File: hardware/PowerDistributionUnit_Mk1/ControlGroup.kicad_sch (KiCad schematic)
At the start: 12 parts, among them U7 74LVC594APW,118

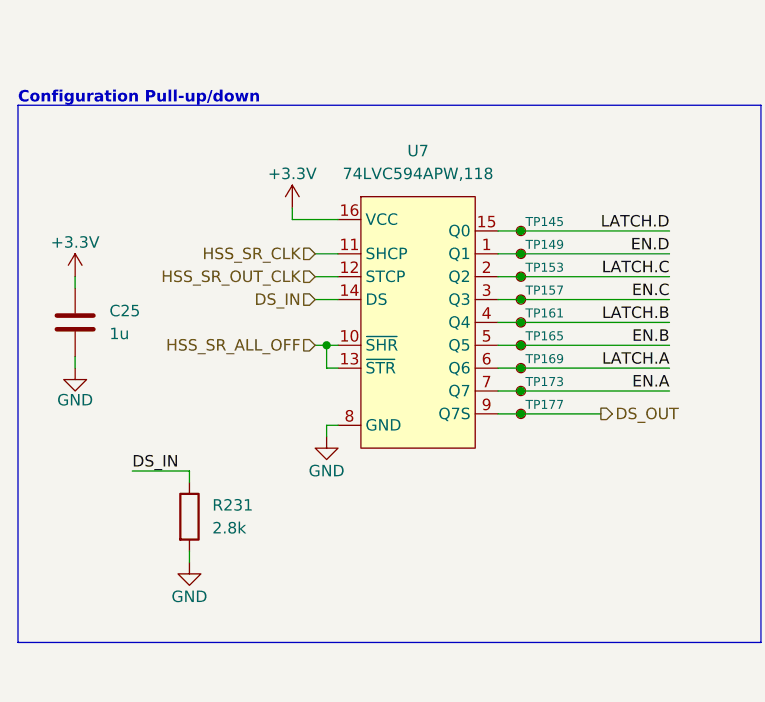
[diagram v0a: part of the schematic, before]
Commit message: BBPDU Mk1 RevB (#6)
* update adc reference to use internal reference (open) with jumper option

* change ADC - reading voltage to resistor divider with option to reference to GND or 1.65V

* change ADC AVDD and AGND connections to regular 3.3V and GND

* make input protection use b2b FETs

* update KiCad-Sharepoint

* update LeaderSOM symbol and SPI pinout (bottom) - need to swap SPI2 and SPI3 names, remove local library copy of LeaderSOM symbol

* change LSOM footprint to centered LSOM footprint, make centered LSOM footprint plated to address hidden pins on LSOM symbol

* update PCB from schematic

* layout/routing for input protection

* fix centered LSOM footprint 3D model, update footprint

* reroute LSOM SPI connections, repin logic analyzer connections

* reroute updated AVDD and AGND on ADCs

* reroute ADCIN- connections to resistor divider from 3.3VA (for 1.65V or 0V)

* change jumper to DNP resistor for ADC reference, routed

* route a couple of missed connections (LV in connection to input prot IC, LV sense connection)

* address DRC

* fix silkscreen labelling issues

* add SRCLK_ENed connection to logic analyzer connector

* silkscreen fixes and stuff

* update rev and year label

* address DRC

* update schematic documentation, clean up, update titleblocks

* add LCSC P/N to libs

* update all symbols with LCSC P/N

* update PCB with LCSC P/Ns

* add center mounting hole

* correct SR part number to SOIC package

* correct fuse table

* change lv sense rdiv values to avoid extended components, update all pull-ups/-downs using 2.8k

* rotate nanofits for inwards clip

* NC the mounting holes (because Lakshay Gupta)

* fix shorted nets error from wrong size res symbol from resistor change

* address DRC

* assembly setup, change latch pull resistor DNP to latch off instead of auto retry by default

* silkscreen stuff

* change DNP for HSS diagnostics to default to current

* change DNP to disable HSS diagnostics by default (primarily use external current 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
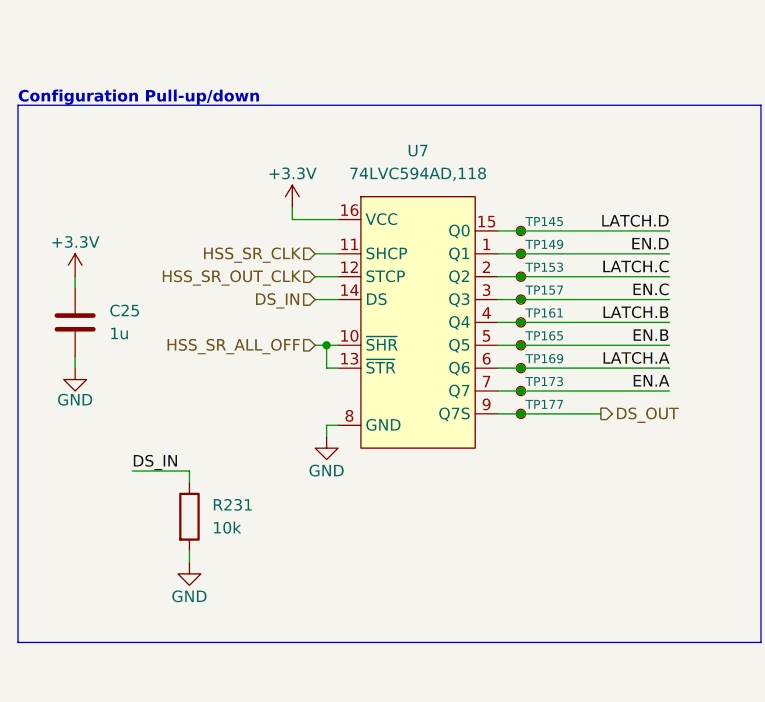
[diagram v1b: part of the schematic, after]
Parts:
- C25: LCSC P/N (none) -> C15849
- R231: value 2.8k -> 10k; symbol PowerDistributionUnitResistorLib:2.8k -> PowerDistributionUnitResistorLib:10k; LCSC P/N (none) -> C25804; Mouser P/N 71-CRCW0603-2.8K-E3 -> 71-CRCW060310K0FKEI; P/N CRCW06032K80FKEA -> CRCW060310K0FKEI
- U7: value 74LVC594APW,118 -> 74LVC594AD,118; symbol PowerDistributionUnitLib:74LVC594APW,118 -> PowerDistributionUnitLib:74LVC594AD,118; Digikey P/N 1727-6687-1-ND -> 1727-74LVC594AD,118CT-ND; LCSC P/N (none) -> C548827; Mouser P/N 771-LVC594APW118 -> 771-LVC594AD118; P/N 74LVC594APW,118 -> 74LVC594AD,118
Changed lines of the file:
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@@
 	(title_block
 		(title "HSS Control Group")
-		(rev "0")
+		(date "2026-02-28")
+		(rev "B")
 		(company "Longhorn Racing Solar")
 		(comment 1 "Changxu Liu")
@@
 	)
 	(symbol
-		(lib_id "PowerDistributionUnitResistorLib:2.8k")
+		(lib_id "PowerDistributionUnitResistorLib:10k")
 		(at 64.77 102.87 0)
 		(unit 1)
@@
 			)
 		)
-		(property "Value" "2.8k"
+		(property "Value" "10k"
 			(at 67.31 104.1399 0)
 			(effects
@@
 			)
 		)
-		(property "P/N" "CRCW06032K80FKEA"
+		(property "P/N" "CRCW060310K0FKEI"
 			(at 64.77 102.87 0)
 			(effects
@@
 			)
 		)
-		(property "Mouser P/N" "71-CRCW0603-2.8K-E3"
+		(property "Mouser P/N" "71-CRCW060310K0FKEI"
 			(at 64.77 102.87 0)
 			(effects
@@
 		)
 		(property "Digikey P/N" "541-2.80KHCT-ND"
+			(at 64.77 102.87 0)
+			(effects
+				(font
+					(size 1.27 1.27)
+				)
+				(hide yes)
+			)
+		)
+		(property "LCSC P/N" "C25804"
 			(at 64.77 102.87 0)
 			(effects
@@
 	)
 	(symbol
-		(lib_id "PowerDistributionUnitLib:74LVC594APW,118")
+		(lib_id "PowerDistributionUnitLib:74LVC594AD,118")
 		(at 90.17 81.28 0)
 		(unit 1)
@@
 			)
 		)
-		(property "Value" "74LVC594APW,118"
+		(property "Value" "74LVC594AD,118"
 			(at 90.17 64.77 0)
 			(effects
@@
 			)
 		)
-		(property "P/N" "74LVC594APW,118"
+		(property "P/N" "74LVC594AD,118"
 			(at 90.17 81.28 0)
 			(effects
@@
 			)
 		)
-		(property "Mouser P/N" "771-LVC594APW118"
+		(property "Mouser P/N" "771-LVC594AD118"
 			(at 90.17 81.28 0)
 			(effects
@@
 			)
 		)
-		(property "Digikey P/N" "1727-6687-1-ND"
+		(property "Digikey P/N" "1727-74LVC594AD,118CT-ND"
+			(at 90.17 81.28 0)
+			(effects
+				(font
+					(size 1.27 1.27)
+				)
+				(hide yes)
+			)
+		)
+		(property "LCSC P/N" "C548827"
 			(at 90.17 81.28 0)
 			(effects
@@
 			(at 52.07 81.28 0)
 			(effects
+				(font
+					(size 1.27 1.27)
+				)
+				(hide yes)
+			)
+		)
+		(property "LCSC P/N" "C15849"
+			(at 52.07 81.28 0)
+			(effects
